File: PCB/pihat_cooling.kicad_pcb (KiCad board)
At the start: 2 copper layers, 65 x 56 mm, 48 parts, among them J1 Barrel_Jack, J2 Conn_01x03, M1 Fan, P1 Conn_02x20_Odd_Even, Q1 AO3401A, Q2 MMBT3906, Q3 AO3401A, Q4 MMBT3904, U1 LM2596S-5

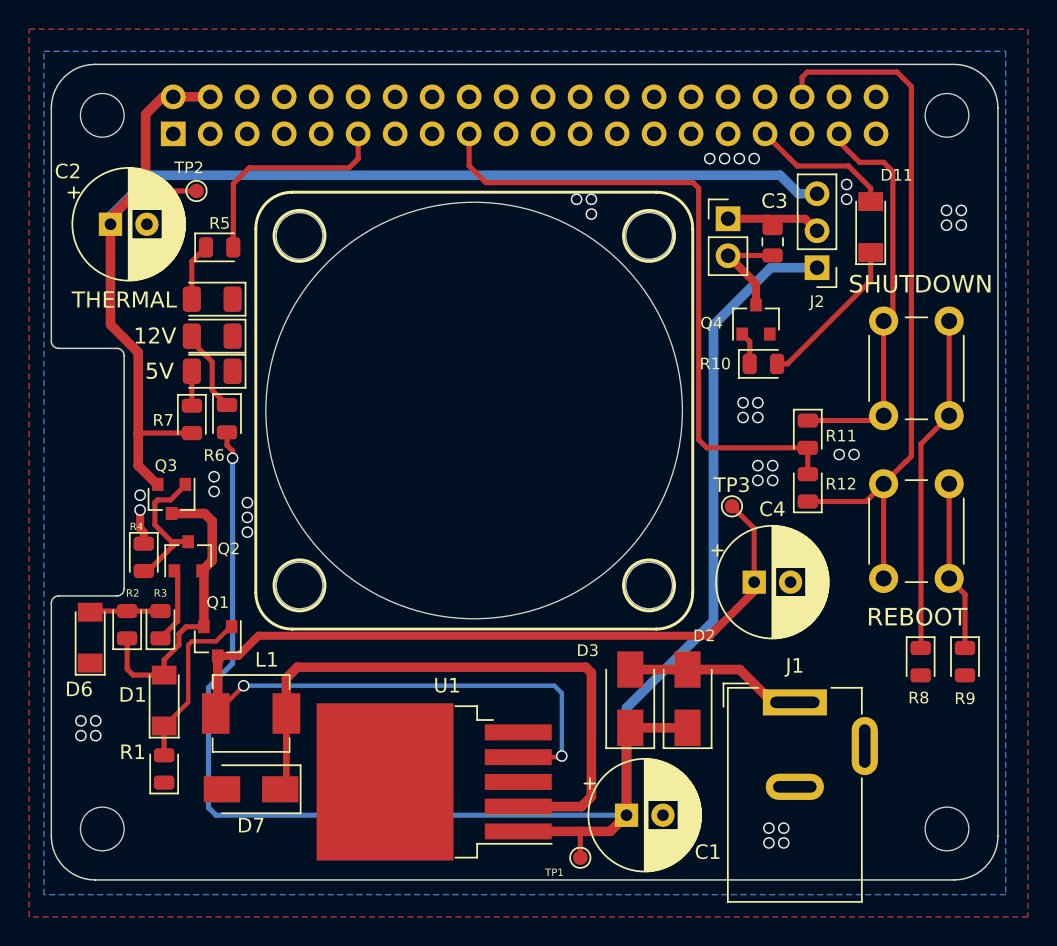
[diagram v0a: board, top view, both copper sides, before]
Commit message: [PCB] change feedback from mosfet output
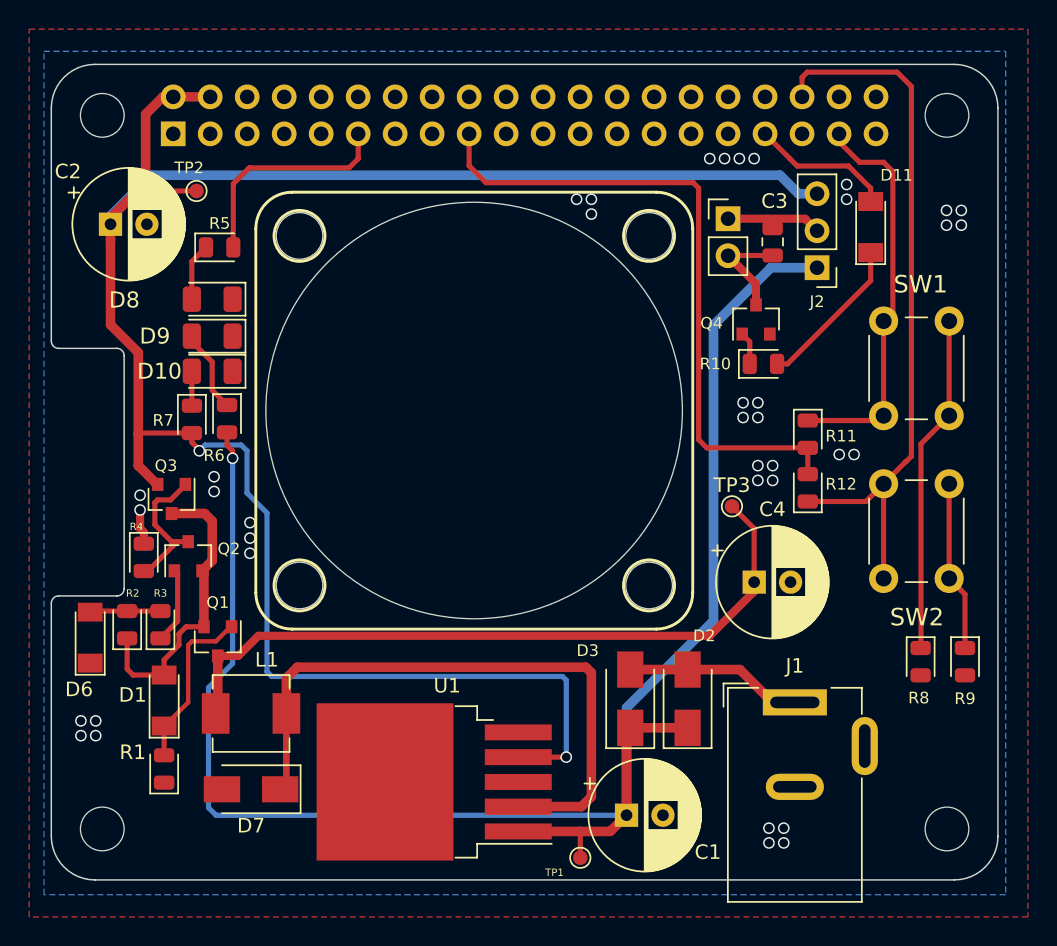
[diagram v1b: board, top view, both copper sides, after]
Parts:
- renumbered 5V to D10, THERMAL to D8, 12V to D9, SHUTDOWN to SW1, REBOOT to SW2
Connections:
- P1 pad 10: (no net) -> Net-(P1-Pad10)
- P1 pad 12: (no net) -> Net-(P1-Pad12)
- P1 pad 13: (no net) -> Net-(P1-Pad13)
- P1 pad 15: (no net) -> Net-(P1-Pad15)
- P1 pad 16: (no net) -> Net-(P1-Pad16)
- P1 pad 18: (no net) -> Net-(P1-Pad18)
- P1 pad 19: (no net) -> Net-(P1-Pad19)
- P1 pad 21: (no net) -> Net-(P1-Pad21)
- P1 pad 22: (no net) -> Net-(P1-Pad22)
- P1 pad 23: (no net) -> Net-(P1-Pad23)
- P1 pad 24: (no net) -> Net-(P1-Pad24)
- P1 pad 26: (no net) -> Net-(P1-Pad26)
- P1 pad 27: (no net) -> /ID_SD
- P1 pad 28: (no net) -> /ID_SC
- P1 pad 29: (no net) -> Net-(P1-Pad29)
- P1 pad 3: (no net) -> Net-(P1-Pad3)
- P1 pad 31: (no net) -> Net-(P1-Pad31)
- P1 pad 32: (no net) -> Net-(P1-Pad32)
- P1 pad 35: (no net) -> Net-(P1-Pad35)
- P1 pad 38: (no net) -> Net-(P1-Pad38)
- P1 pad 40: (no net) -> Net-(P1-Pad40)
- P1 pad 5: (no net) -> Net-(P1-Pad5)
- P1 pad 7: (no net) -> Net-(P1-Pad7)
- P1 pad 8: (no net) -> Net-(P1-Pad8)
- U1 pad 4: +5V -> +5VP
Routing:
- net +5VP: track 91.1 -> 141.2 mm, vias 0 -> 2
- net +5V: track 81.4 -> 49.3 mm, vias 2 -> 0

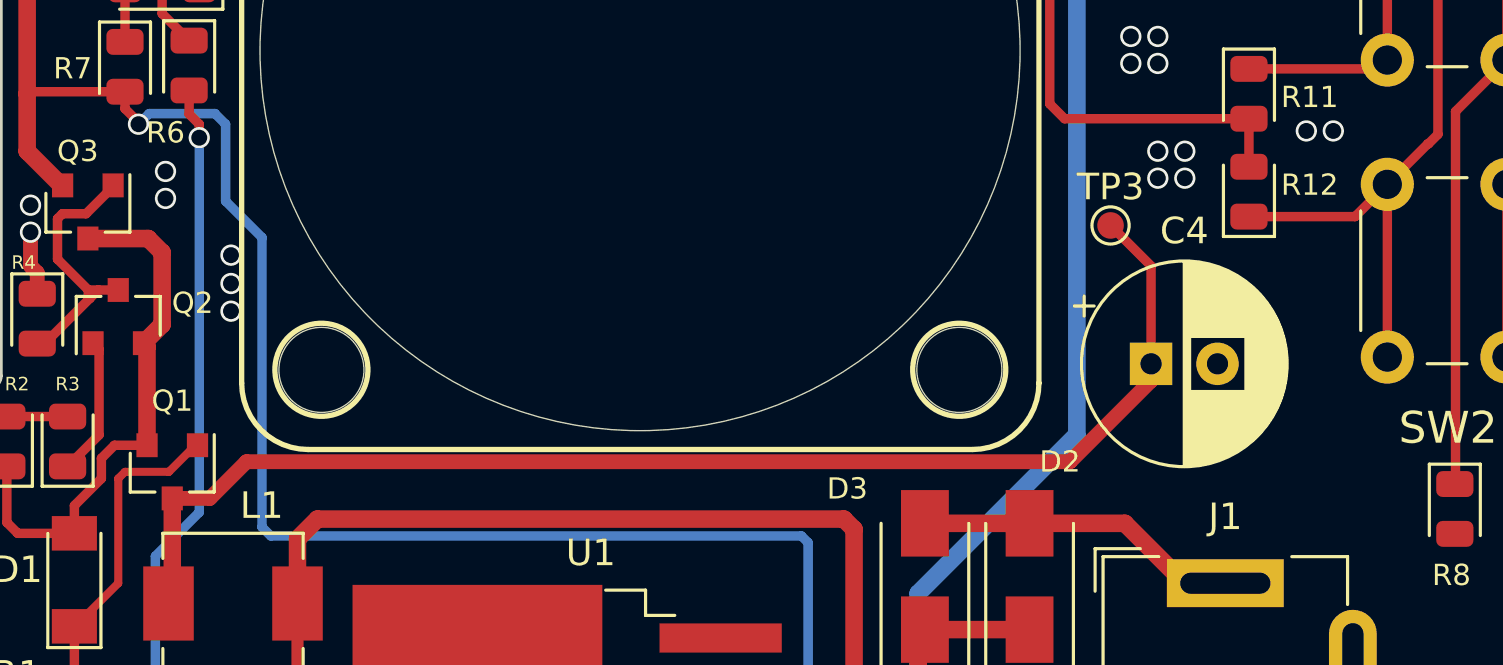
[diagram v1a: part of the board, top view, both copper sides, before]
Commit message: [PCB] delete 5V capacitor + add open hardware symbol
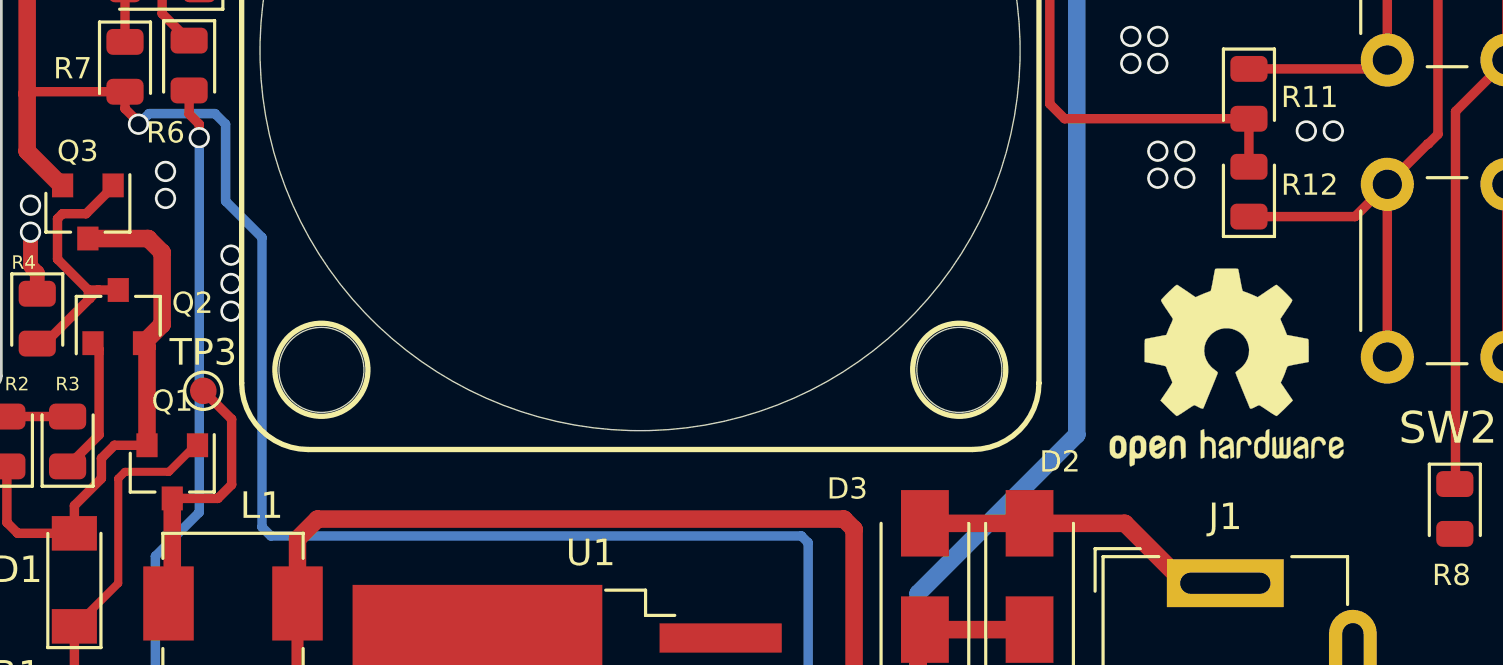
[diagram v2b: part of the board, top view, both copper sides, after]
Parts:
- removed C4: CP, Capacitor_THT:CP_Radial_D7.5mm_P2.50mm
- added REF**: OSHW-Logo2_9.8x8mm_SilkScreen, Symbol:OSHW-Logo2_9.8x8mm_SilkScreen, F.Cu at (251.1, 129.7)
- moved TP3 34.7 mm to (212.6, 130.6)
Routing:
- net +5V: track 49.3 -> 10.4 mm
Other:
- board text added: "PiHat_Cooling_V1.0"

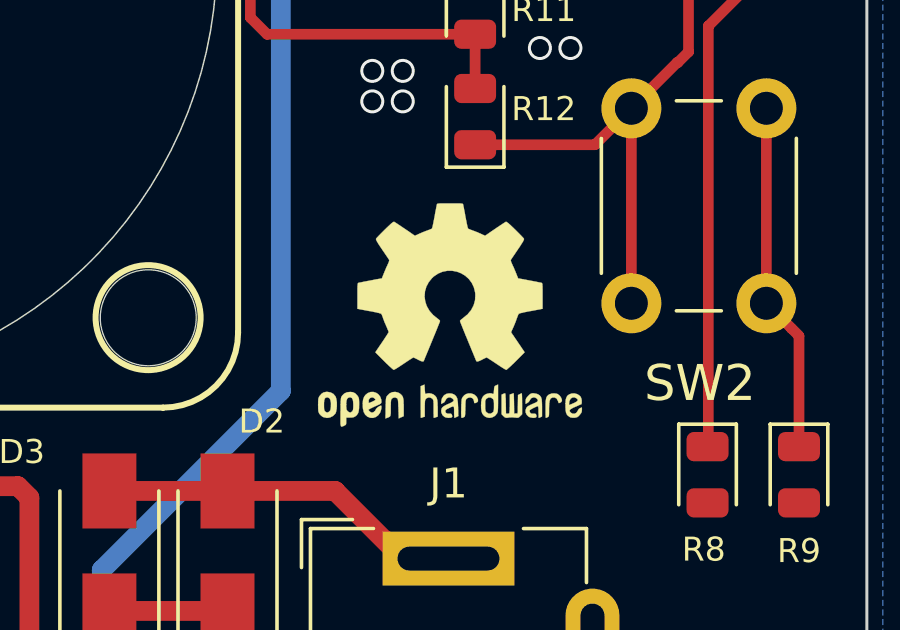
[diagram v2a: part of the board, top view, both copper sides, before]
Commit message: [PCB] update pcb for new resistors value
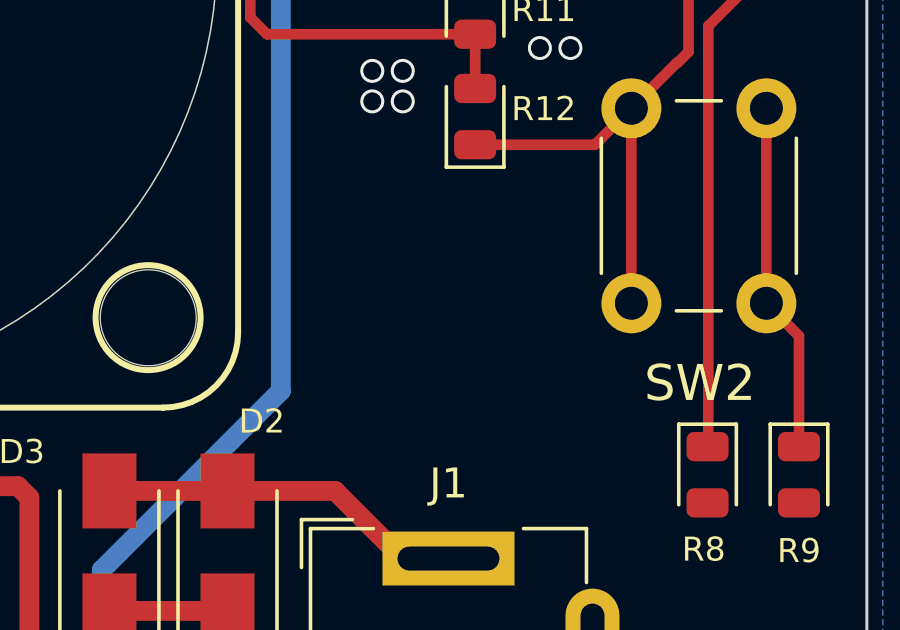
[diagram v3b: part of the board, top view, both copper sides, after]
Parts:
- removed REF**: OSHW-Logo2_9.8x8mm_SilkScreen, Symbol:OSHW-Logo2_9.8x8mm_SilkScreen
- R6: value 1K -> 5K
- R7: value 1K -> 3K
